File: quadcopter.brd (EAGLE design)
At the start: 138 x 138 mm, 98 parts, among them J1 AVR_SPI_PRG_6NS, M1 MOTOR_PADS, M2 MOTOR_PADS, M3 MOTOR_PADS, M4 MOTOR_PADS, SW1 PUSHBUTTON_SMD-VERTICAL-1, U1 ATMEGA128RFA1, U2 IMU_LSM9DS1TR, Y1 16MHz

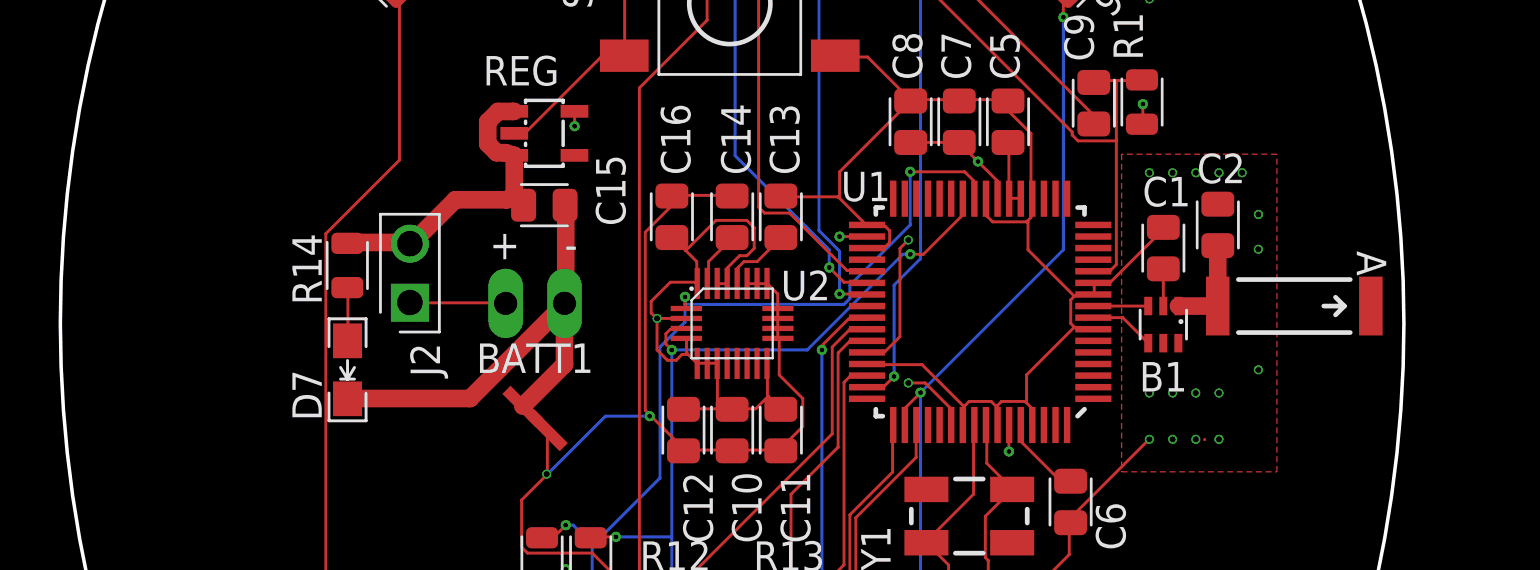
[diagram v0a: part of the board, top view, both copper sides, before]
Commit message: Added logo on board
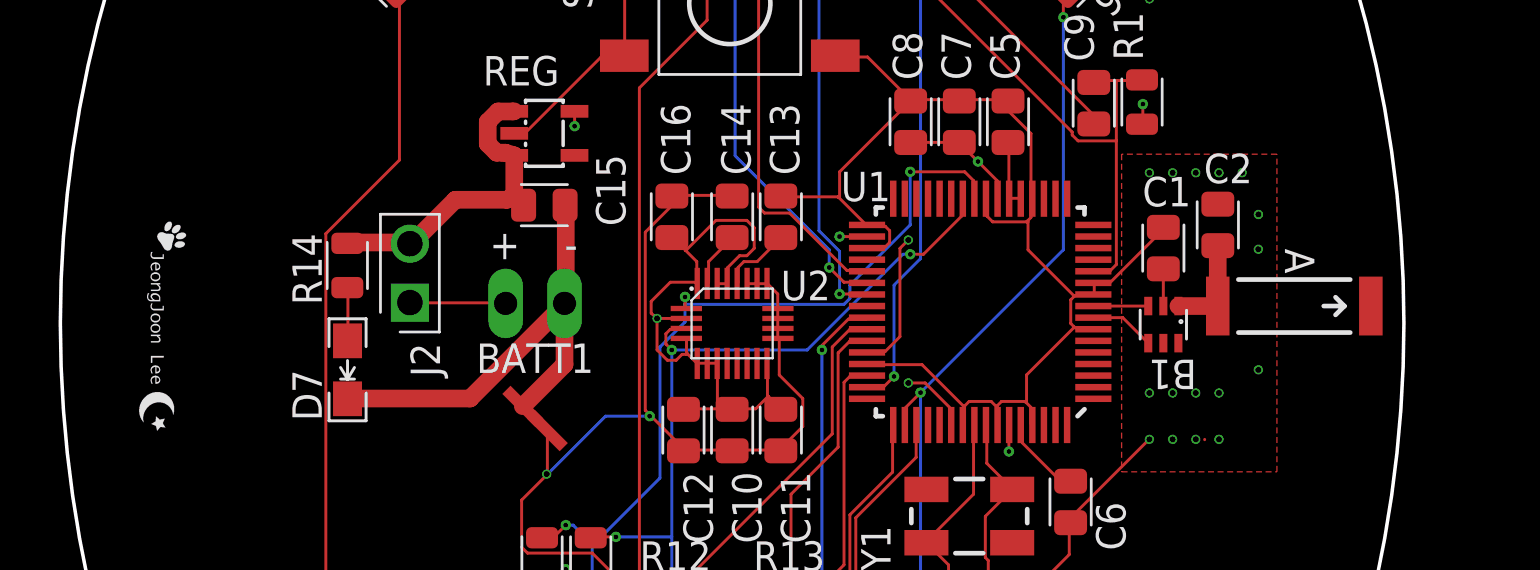
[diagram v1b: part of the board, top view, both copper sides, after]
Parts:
- added LOGO: (no value), logo:LOGO
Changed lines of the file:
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@@
 <layers>
 <layer number="1" name="Top" color="4" fill="1" visible="yes" active="yes"/>
-<layer number="2" name="Route2" color="1" fill="3" visible="yes" active="yes"/>
+<layer number="2" name="Route2" color="1" fill="3" visible="no" active="yes"/>
 <layer number="3" name="Route3" color="4" fill="3" visible="no" active="no"/>
 <layer number="4" name="Route4" color="1" fill="4" visible="no" active="no"/>
@@
 <layer number="13" name="Route13" color="4" fill="5" visible="no" active="no"/>
 <layer number="14" name="Route14" color="1" fill="6" visible="no" active="no"/>
-<layer number="15" name="Route15" color="4" fill="6" visible="yes" active="yes"/>
+<layer number="15" name="Route15" color="4" fill="6" visible="no" active="yes"/>
 <layer number="16" name="Bottom" color="1" fill="1" visible="yes" active="yes"/>
 <layer number="17" name="Pads" color="2" fill="1" visible="yes" active="yes"/>
@@
 <attribute name="MFR" value="Linx Technologies Inc." x="24.25" y="0.75" size="1.778" layer="27" display="off"/>
 <attribute name="MPN" value="ANT-2.45-CHP-T" x="24.25" y="0.75" size="1.778" layer="27" display="off"/>
-<attribute name="NAME" x="27.581" y="2.59" size="1.27" layer="25" font="vector" rot="SR270" align="center"/>
+<attribute name="NAME" x="24.481" y="2.69" size="1.27" layer="25" font="vector" rot="SR270" align="center"/>
 <attribute name="PRICE" value="3.16" x="24.25" y="0.75" size="1.778" layer="27" display="off"/>
 <attribute name="REVIEWER" value="Swanson" x="24.25" y="0.75" size="1.778" layer="27" display="off"/>
 </element>
-<element name="B1" library="quadparts_prebuilt" package="BALUN" value="BALUN0805" x="18.6" y="-0.05" rot="R180">
+<element name="B1" library="quadparts_prebuilt" package="BALUN" value="BALUN0805" x="18.6" y="-0.05" smashed="yes" rot="R180">
 <attribute name="CREATOR" value="Swanson" x="18.6" y="-0.05" size="1.778" layer="27" rot="R180" display="off"/>
 <attribute name="DATASHEET" value="http://katalog.we-online.de/pbs/datasheet/748421245.pdf" x="18.6" y="-0.05" size="1.778" layer="27" rot="R180" display="off"/>
@@
 <attribute name="MFR" value="Wurth Electronics Inc" x="18.6" y="-0.05" size="1.778" layer="27" rot="R180" display="off"/>
 <attribute name="MPN" value="748421245" x="18.6" y="-0.05" size="1.778" layer="27" rot="R180" display="off"/>
+<attribute name="NAME" x="19" y="-2.2" size="1.27" layer="25" font="vector" rot="SR180" align="center"/>
 <attribute name="PRICE" value="2.63" x="18.6" y="-0.05" size="1.778" layer="27" rot="R180" display="off"/>
 <attribute name="REVIEWER" value="Swanson" x="18.6" y="-0.05" size="1.778" layer="27" rot="R180" display="off"/>
@@
 <attribute name="MFR" value="Murata Electronics North America" x="20.95" y="4.25" size="1.778" layer="27" rot="R90" display="off"/>
 <attribute name="MPN" value="GQM2195C2AR75CB01D" x="20.95" y="4.25" size="1.778" layer="27" rot="R90" display="off"/>
-<attribute name="NAME" x="20.05" y="6.05" size="1.27" layer="25" font="vector"/>
+<attribute name="NAME" x="20.35" y="6.05" size="1.27" layer="25" font="vector"/>
 <attribute name="REVIEWER" value="Swanson" x="20.95" y="4.25" size="1.778" layer="27" rot="R90" display="off"/>
 <attribute name="VALUE" x="20.95" y="4.25" size="1.2" layer="27" font="vector" ratio="10" rot="R90"/>
@@
 <attribute name="DISTPN" value="NA" x="21" y="-5" size="1.778" layer="27" display="off"/>
 </element>
+<element name="LOGO" library="logo" package="LOGO" value="" x="-25.6" y="4.4" rot="R270"/>
 </elements>
 <signals>
@@
 <vertex x="-4.3" y="2.8"/>
 <vertex x="3" y="2.8"/>
-<vertex x="3" y="-2.7"/>
-<vertex x="-3" y="-2.7"/>
+<vertex x="3" y="-2.8"/>
+<vertex x="-3" y="-2.8"/>
 <vertex x="-3" y="2.2"/>
 <vertex x="-4.3" y="2.2"/>
@@
 <vertex x="-4.3" y="2.8"/>
 <vertex x="3" y="2.8"/>
-<vertex x="3" y="-2.7"/>
-<vertex x="-3" y="-2.7"/>
+<vertex x="3" y="-2.8"/>
+<vertex x="-3" y="-2.8"/>
 <vertex x="-3" y="2.2"/>
 <vertex x="-4.3" y="2.2"/>

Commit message: Redesigned board
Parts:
- removed V3: (no value), quadparts_prebuilt:VIA-0.254MM
- added V2, V35, V36, V4: (no value), custom:VIA_0.454
- moved LOGO 6.10 mm to (-25.6, 10.5), turned to 0 degrees
- moved V1 4.88 mm to (7.60, -1.27)
- moved C16 4.41 mm to (-4.50, 8.57)
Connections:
- net 3V: no longer V3.P1
- net GND: now also V2.VIA, V35.VIA, V36.VIA, V4.VIA
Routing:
- net GND: track 196.2 -> 190.1 mm
- net 3V: track 48.6 -> 51.1 mm, vias 6 -> 5
